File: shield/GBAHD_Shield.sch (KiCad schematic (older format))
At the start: 50 parts, among them J1 Conn_01x40, J10 Conn_01x02, J11 Conn_01x05, J2 Conn_02x08_Top_Bottom, J3 Conn_01x20, J4 Conn_02x10_Top_Bottom, J5 Conn_01x34, J6 Conn_02x03_Odd_Even, J7 Conn_01x32, J8 Conn_01x05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

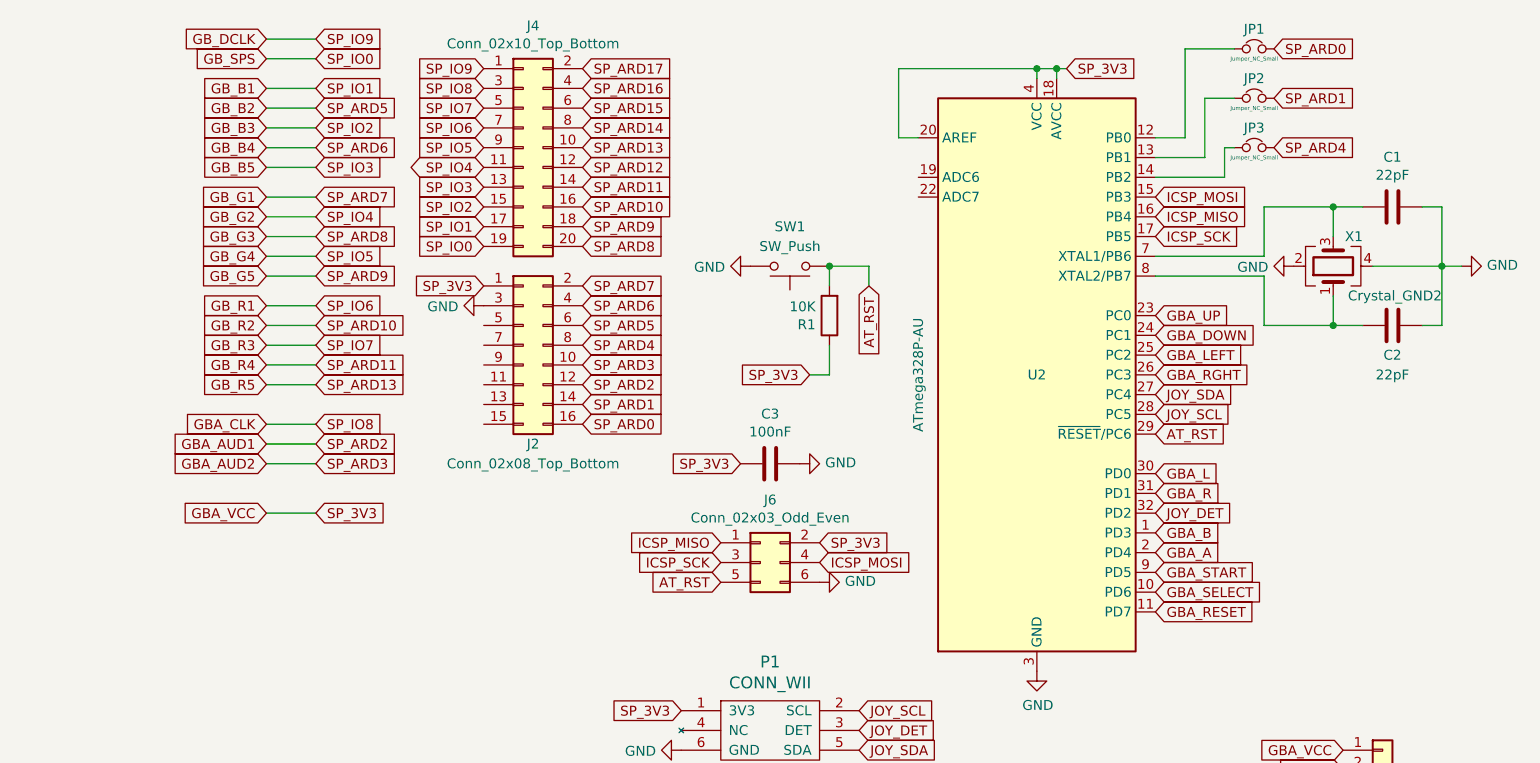
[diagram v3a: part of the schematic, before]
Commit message: Updated board files to include new trace.
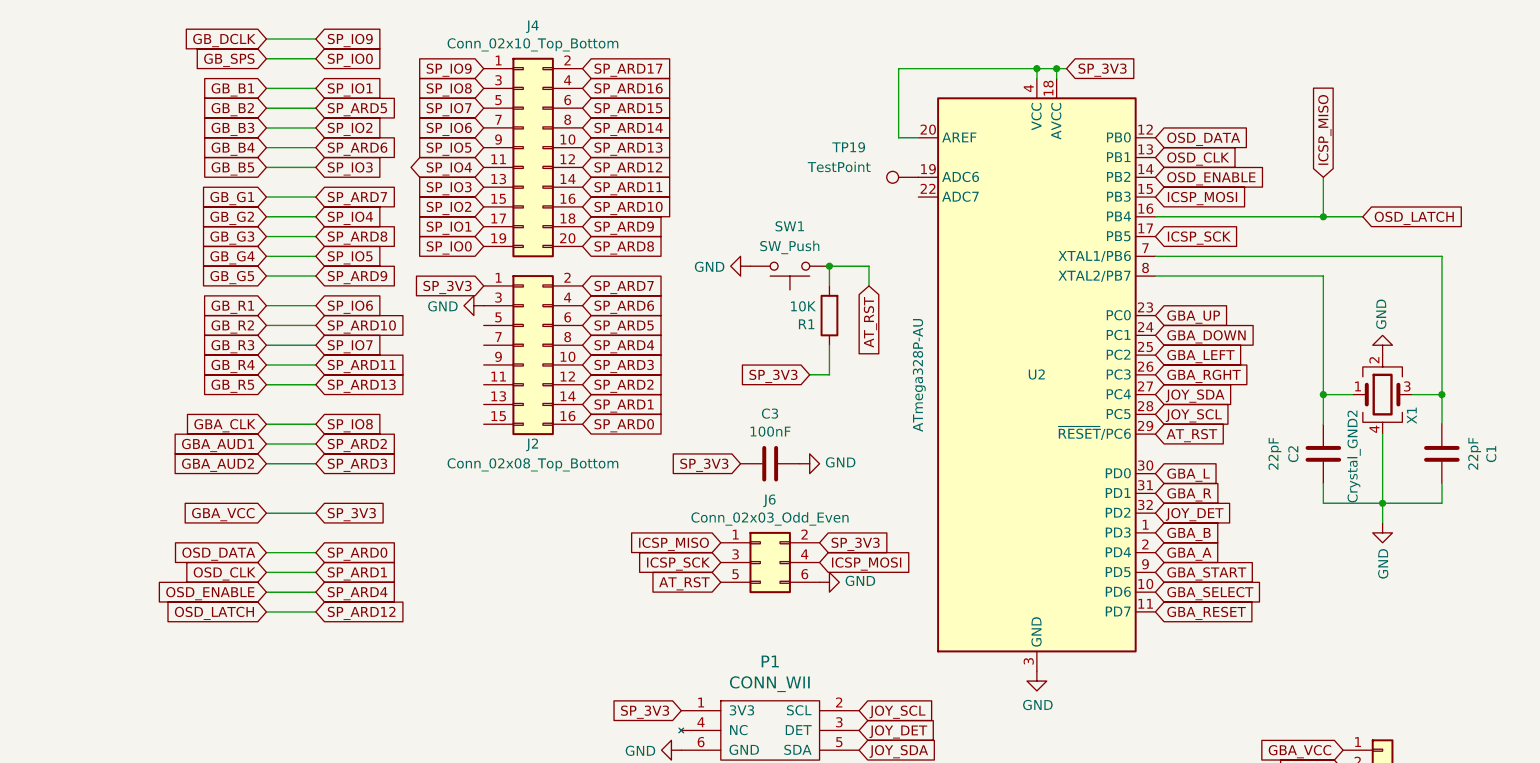
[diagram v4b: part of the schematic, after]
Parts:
- removed JP1, JP2, JP3: Jumper_NC_Small, Jumper:SolderJumper-2_P1.3mm_Bridged_RoundedPad1.0x1.5mm, symbol Device:Jumper_NC_Small
- added TP19: TestPoint, Raizu_OFFSET:SOLDER_PAD, symbol Connector:TestPoint
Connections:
- net SP_ARD0 is gone; now on net OSD_DATA: J2.16 (Pin_16)
- net SP_ARD1 is gone; now on net OSD_CLK: J2.14 (Pin_14)
- net SP_ARD12 is gone; now on net ICSP_MISO: J4.12 (Pin_12)
- net SP_ARD4 is gone; now on net OSD_ENABLE: J2.8 (Pin_8)
- net OSD_DATA: now reaches U2.12 (PB0)
- net OSD_CLK: now reaches U2.13 (PB1)
- net OSD_ENABLE: now reaches U2.14 (PB2)
- net at U2.19 (ADC6): now also TP19.1
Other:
- moved on the sheet: C1, C2, X1
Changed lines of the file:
@@
 L Device:C C1
 U 1 1 5FFC1902
-P 10600 1600
-F 0 "C1" V 10348 1600 50  0000 C CNN
-F 1 "22pF" V 10439 1600 50  0000 C CNN
-F 2 "Capacitor_SMD:C_0805_2012Metric_Pad1.18x1.45mm_HandSolder" H 10638 1450 50  0001 C CNN
-F 3 "~" H 10600 1600 50  0001 C CNN
-	1    10600 1600
-	0    1    1    0
+P 10850 2850
+F 0 "C1" V 10598 2850 50  0000 C CNN
+F 1 "22pF" V 10689 2850 50  0000 C CNN
+F 2 "Capacitor_SMD:C_0805_2012Metric_Pad1.18x1.45mm_HandSolder" H 10888 2700 50  0001 C CNN
+F 3 "~" H 10850 2850 50  0001 C CNN
+	1    10850 2850
+	-1   0    0    1
 $EndComp
 $Comp
 L Device:C C2
 U 1 1 5FFC247D
-P 10600 2200
-F 0 "C2" V 10750 2200 50  0000 C CNN
-F 1 "22pF" V 10850 2200 50  0000 C CNN
-F 2 "Capacitor_SMD:C_0805_2012Metric_Pad1.18x1.45mm_HandSolder" H 10638 2050 50  0001 C CNN
-F 3 "~" H 10600 2200 50  0001 C CNN
-	1    10600 2200
-	0    1    1    0
+P 10250 2850
+F 0 "C2" V 10400 2850 50  0000 C CNN
+F 1 "22pF" V 10500 2850 50  0000 C CNN
+F 2 "Capacitor_SMD:C_0805_2012Metric_Pad1.18x1.45mm_HandSolder" H 10288 2700 50  0001 C CNN
+F 3 "~" H 10250 2850 50  0001 C CNN
+	1    10250 2850
+	-1   0    0    1
 $EndComp
 Text GLabel 4900 2700 0    50   Input ~ 0
@@
 	0    -1   -1   0
 $EndComp
-Text GLabel 9400 1650 2    50   Input ~ 0
+Text GLabel 10250 1450 1    50   Input ~ 0
 ICSP_MISO
 Text GLabel 9400 1750 2    50   Input ~ 0
@@
 Text GLabel 7700 3300 2    50   Input ~ 0
 SP_3V3
-Wire Wire Line
-	9400 1850 9950 1850
-Wire Wire Line
-	9400 1950 9950 1950
 $Comp
 L power:GND #PWR0105
@@
 GBA_SELECT
 Wire Wire Line
-	9950 1950 9950 2200
-Wire Wire Line
-	10850 1900 10850 1600
-Wire Wire Line
-	10850 1600 10750 1600
-Wire Wire Line
-	10850 1900 10850 2200
-Wire Wire Line
-	10850 2200 10750 2200
-Connection ~ 10850 1900
-Wire Wire Line
-	10850 1900 10950 1900
+	10550 3100 10850 3100
+Wire Wire Line
+	10850 3100 10850 3000
+Wire Wire Line
+	10550 3100 10250 3100
+Wire Wire Line
+	10250 3100 10250 3000
+Connection ~ 10550 3100
+Wire Wire Line
+	10550 3100 10550 3200
 $Comp
 L power:GND #PWR0104
 U 1 1 60021E7C
-P 10950 1900
-F 0 "#PWR0104" H 10950 1650 50  0001 C CNN
-F 1 "GND" V 10955 1772 50  0000 R CNN
-F 2 "" H 10950 1900 50  0001 C CNN
-F 3 "" H 10950 1900 50  0001 C CNN
-	1    10950 1900
-	0    -1   -1   0
+P 10550 3200
+F 0 "#PWR0104" H 10550 2950 50  0001 C CNN
+F 1 "GND" V 10555 3072 50  0000 R CNN
+F 2 "" H 10550 3200 50  0001 C CNN
+F 3 "" H 10550 3200 50  0001 C CNN
+	1    10550 3200
+	1    0    0    -1
 $EndComp
 Text GLabel 10350 4350 0    50   Input ~ 0
@@
 GB_G2
 Wire Wire Line
-	10500 1900 10850 1900
+	10550 2750 10550 3100
 Text GLabel 6000 1400 0    50   BiDi ~ 0
 SP_IO4
@@
 L Device:Crystal_GND24 X1
 U 1 1 5FFD18DB
-P 10300 1900
-F 0 "X1" V 10450 1750 50  0000 L CNN
-F 1 "Crystal_GND2" V 10150 1350 50  0000 L CNN
-F 2 "Crystal:Crystal_SMD_3225-4Pin_3.2x2.5mm" H 10300 1900 50  0001 C CNN
-F 3 "~" H 10300 1900 50  0001 C CNN
-	1    10300 1900
-	0    -1   -1   0
-$EndComp
-Wire Wire Line
-	10300 1750 10300 1600
-Wire Wire Line
-	10300 1600 10450 1600
-Wire Wire Line
-	10300 2050 10300 2200
-Connection ~ 10300 2200
-Wire Wire Line
-	10300 2200 10450 2200
-Wire Wire Line
-	9950 1850 9950 1600
-Wire Wire Line
-	9950 1600 10300 1600
-Connection ~ 10300 1600
-Wire Wire Line
-	9950 2200 10300 2200
+P 10550 2550
+F 0 "X1" V 10700 2400 50  0000 L CNN
+F 1 "Crystal_GND2" V 10400 2000 50  0000 L CNN
+F 2 "Crystal:Crystal_SMD_3225-4Pin_3.2x2.5mm" H 10550 2550 50  0001 C CNN
+F 3 "~" H 10550 2550 50  0001 C CNN
+	1    10550 2550
+	1    0    0    -1
+$EndComp
+Wire Wire Line
+	10700 2550 10850 2550
+Wire Wire Line
+	10850 2550 10850 2700
+Wire Wire Line
+	10400 2550 10250 2550
+Connection ~ 10250 2550
+Wire Wire Line
+	10250 2550 10250 2700
+Connection ~ 10850 2550
 $Comp
 L power:GND #PWR0111
 U 1 1 5FFDA756
-P 10100 1900
-F 0 "#PWR0111" H 10100 1650 50  0001 C CNN
-F 1 "GND" V 10105 1772 50  0000 R CNN
-F 2 "" H 10100 1900 50  0001 C CNN
-F 3 "" H 10100 1900 50  0001 C CNN
-	1    10100 1900
-	0    1    1    0
+P 10550 2350
+F 0 "#PWR0111" H 10550 2100 50  0001 C CNN
+F 1 "GND" V 10555 2222 50  0000 R CNN
+F 2 "" H 10550 2350 50  0001 C CNN
+F 3 "" H 10550 2350 50  0001 C CNN
+	1    10550 2350
+	-1   0    0    1
 $EndComp
 $Comp
@@
 Text GLabel 10350 5250 0    50   Input ~ 0
 GBA_RESET
-Text GLabel 10000 1300 2    50   Input ~ 0
-SP_ARD4
-Text GLabel 10000 1050 2    50   Input ~ 0
-SP_ARD1
-Text GLabel 10000 800  2    50   Input ~ 0
-SP_ARD0
+Text GLabel 9400 1450 2    50   Input ~ 0
+OSD_ENABLE
+Text GLabel 9400 1350 2    50   Input ~ 0
+OSD_CLK
+Text GLabel 9400 1250 2    50   Input ~ 0
+OSD_DATA
 Text GLabel 7900 4150 2    50   Input ~ 0
 JOY_SCL
@@
 JOY_SDA
 $Comp
-L Device:Jumper_NC_Small JP2
-U 1 1 60A5C6EF
-P 9900 1050
-F 0 "JP2" H 9900 1150 50  0000 C CNN
-F 1 "Jumper_NC_Small" H 9900 1000 20  0000 C CNN
-F 2 "Jumper:SolderJumper-2_P1.3mm_Bridged_RoundedPad1.0x1.5mm" H 9900 1050 50  0001 C CNN
-F 3 "~" H 9900 1050 50  0001 C CNN
-	1    9900 1050
-	1    0    0    -1
-$EndComp
-$Comp
-L Device:Jumper_NC_Small JP3
-U 1 1 60A5D830
-P 9900 1300
-F 0 "JP3" H 9900 1400 50  0000 C CNN
-F 1 "Jumper_NC_Small" H 9900 1250 20  0000 C CNN
-F 2 "Jumper:SolderJumper-2_P1.3mm_Bridged_RoundedPad1.0x1.5mm" H 9900 1300 50  0001 C CNN
-F 3 "~" H 9900 1300 50  0001 C CNN
-	1    9900 1300
-	1    0    0    -1
-$EndComp
-$Comp
-L Device:Jumper_NC_Small JP1
-U 1 1 60A5E115
-P 9900 800
-F 0 "JP1" H 9900 900 50  0000 C CNN
-F 1 "Jumper_NC_Small" H 9900 750 20  0000 C CNN
-F 2 "Jumper:SolderJumper-2_P1.3mm_Bridged_RoundedPad1.0x1.5mm" H 9900 800 50  0001 C CNN
-F 3 "~" H 9900 800 50  0001 C CNN
-	1    9900 800
-	1    0    0    -1
-$EndComp
-Wire Wire Line
-	9400 1250 9550 1250
-Wire Wire Line
-	9550 1250 9550 800
-Wire Wire Line
-	9550 800  9800 800
-Wire Wire Line
-	9400 1350 9650 1350
-Wire Wire Line
-	9650 1350 9650 1050
-Wire Wire Line
-	9650 1050 9800 1050
-Wire Wire Line
-	9400 1450 9750 1450
-Wire Wire Line
-	9750 1450 9750 1300
-Wire Wire Line
-	9750 1300 9800 1300
-$Comp
 L Connector_Generic:Conn_01x20 J9
 U 1 1 60AA1942
@@
 Text GLabel 9400 3250 2    50   Input ~ 0
 GBA_B
+Text GLabel 5150 3350 2    50   Input ~ 0
+SP_ARD0
+Text GLabel 4900 3350 0    50   Input ~ 0
+OSD_DATA
+Text GLabel 5150 3450 2    50   Input ~ 0
+SP_ARD1
+Text GLabel 4900 3450 0    50   Input ~ 0
+OSD_CLK
+Text GLabel 10450 1650 2    50   Input ~ 0
+OSD_LATCH
+Text GLabel 5150 3550 2    50   Input ~ 0
+SP_ARD4
+Text GLabel 4900 3550 0    50   Input ~ 0
+OSD_ENABLE
+Text GLabel 5150 3650 2    50   Input ~ 0
+SP_ARD12
+Text GLabel 4900 3650 0    50   Input ~ 0
+OSD_LATCH
+Wire Wire Line
+	4900 3350 5150 3350
+Wire Wire Line
+	5150 3450 4900 3450
+Wire Wire Line
+	4900 3550 5150 3550
+Wire Wire Line
+	5150 3650 4900 3650
+$Comp
+L Connector:TestPoint TP19
+U 1 1 60AD9813
+P 8200 1450
+F 0 "TP19" V 8350 1800 50  0000 C CNN
+F 1 "TestPoint" V 8250 1850 50  0000 C CNN
+F 2 "Raizu_OFFSET:SOLDER_PAD" H 8400 1450 50  0001 C CNN
+F 3 "~" H 8400 1450 50  0001 C CNN
+	1    8200 1450
+	0    -1   -1   0
+$EndComp
+Wire Wire Line
+	9400 1850 10850 1850
+Wire Wire Line
+	10850 1850 10850 2550
+Wire Wire Line
+	9400 1950 10250 1950
+Wire Wire Line
+	10250 1950 10250 2550
+Wire Wire Line
+	9400 1650 10250 1650
+Wire Wire Line
+	10250 1650 10250 1450
+Wire Wire Line
+	10250 1650 10450 1650
+Connection ~ 10250 1650
 $EndSCHEMATC
